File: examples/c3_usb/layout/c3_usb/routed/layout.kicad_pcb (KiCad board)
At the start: 2 copper layers, 40 x 30 mm, 19 parts, among them J1 TYPE-C-31-M-12, U1 ESP32-C3-MINI-1-N4, U2 AP2112K-3.3TRG1, U3 USBLC6-2SC6, U4 B3U-1000P, U5 B3U-1000P

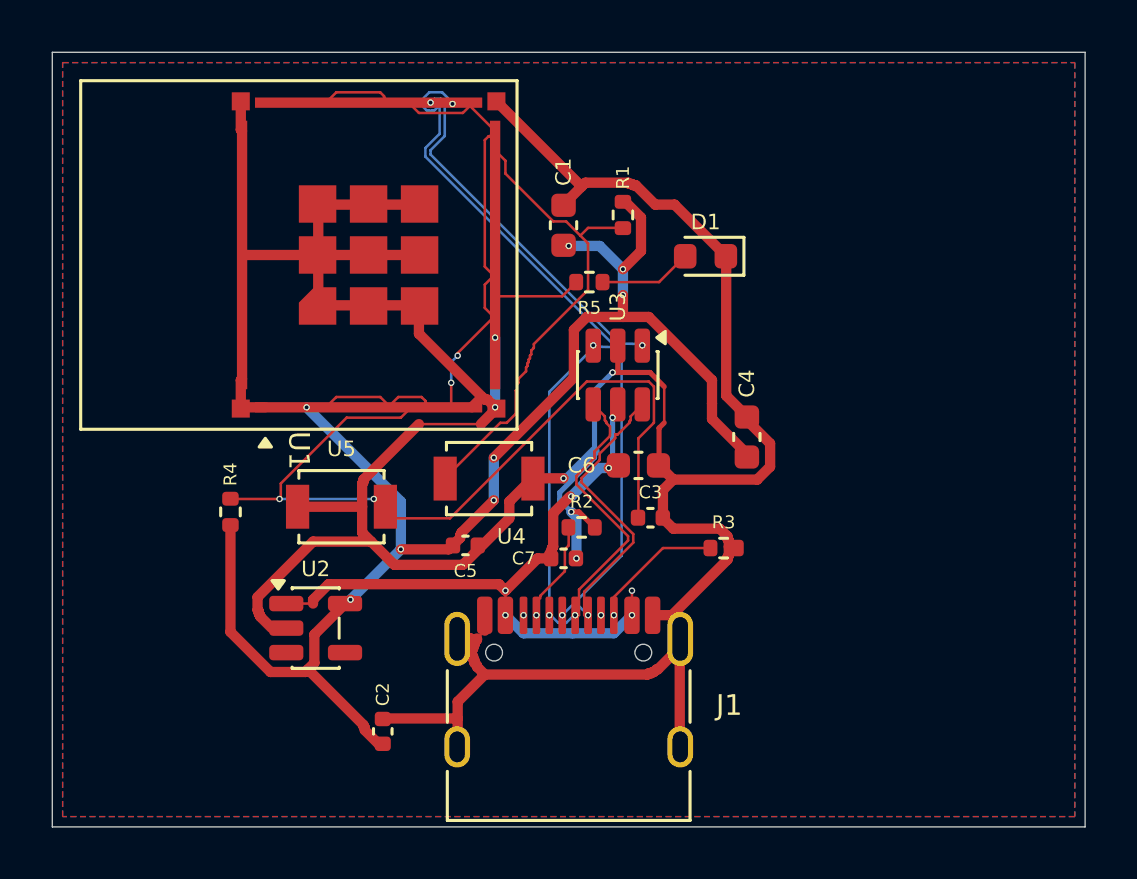
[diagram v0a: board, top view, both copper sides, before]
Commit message: Gate Standard fab: no 0603 via-in-pad, pad-pad place check, compiled vias.
Place check now fails different-net pads closer than the copper floor
(NTC-on-Teensy would have been ok). Cluster no longer moves U* or
parks parts off the outline.

Route forbids via-in-pad on the maze (--same-net-pad-clearance),
passes compiled 0.45/0.20 vias, and on 4-layer runs a GND tap pass so
HTSSOP PGND pins dog-bone. USB-C underpad fanout stays 0.25/0.15.

Fab fails via-in-pad on passives and mounting pegs, quotes grouped BOM
designators, omits through-hole without LCSC, skips fiducials that sit
on a courtyard, and grades 4-layer DRC at JLCPCB 0.127 mm. max_mm is
an airwire budget, not a KiCad maze-length rule.

Re-route examples/c3_usb so the kicad fab job still has USB-C underpad
vias and zero 0603 via-in-pad.
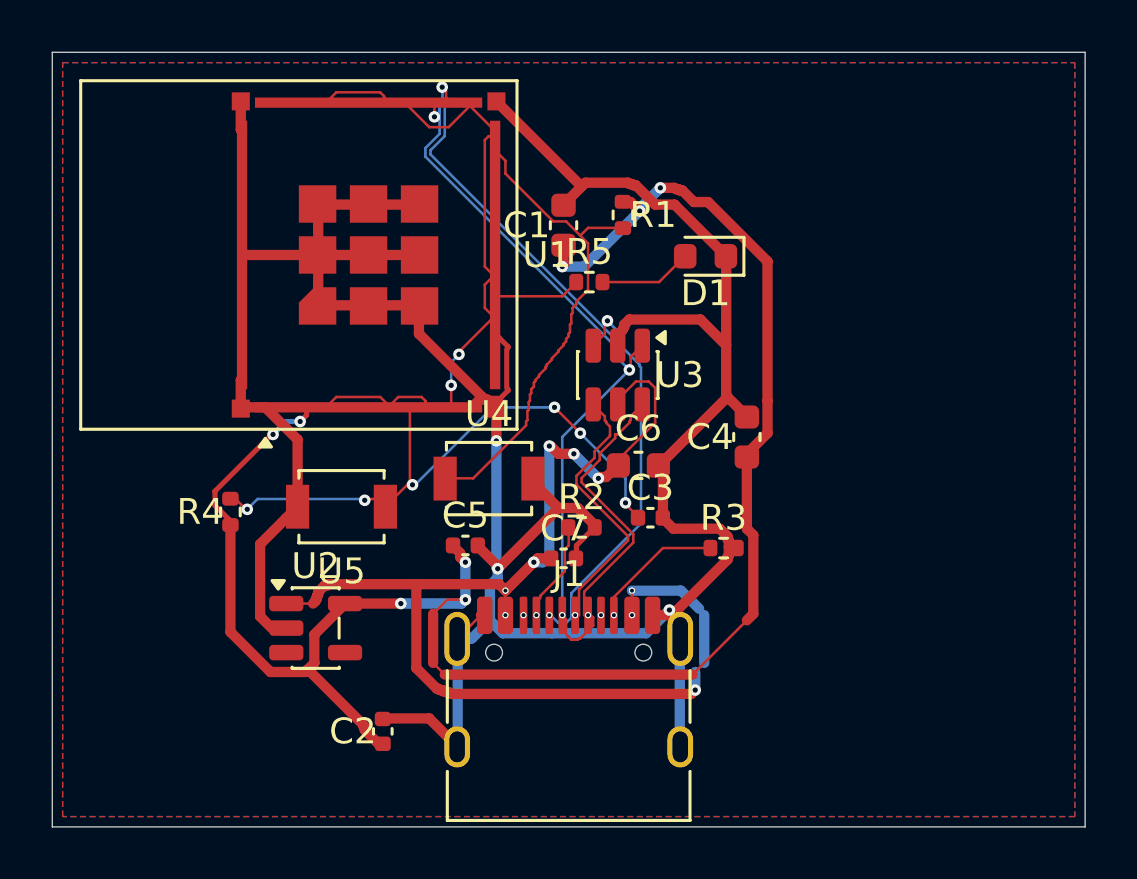
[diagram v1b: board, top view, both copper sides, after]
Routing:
- net VBUS: track 26.4 -> 48.1 mm, vias 7 -> 9
- net 3V3: track 55.5 -> 71.7 mm
- net GND: track 134.7 -> 121.1 mm, vias 6 -> 3
- net EN: track 30.6 -> 23.0 mm, vias 2 -> 6
- net USB_DP: track 37.3 -> 40.2 mm
- net USB_DN: track 39.5 -> 40.1 mm
